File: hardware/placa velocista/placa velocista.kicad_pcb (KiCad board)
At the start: 2 copper layers, 103.6 x 74.9 mm, 22 parts, among them J1 Conn_01x07, J5 Screw_Terminal_01x02, SW2 SW_SPDT, SW3 s, U1 ESP32_CDN, U2 LM7805

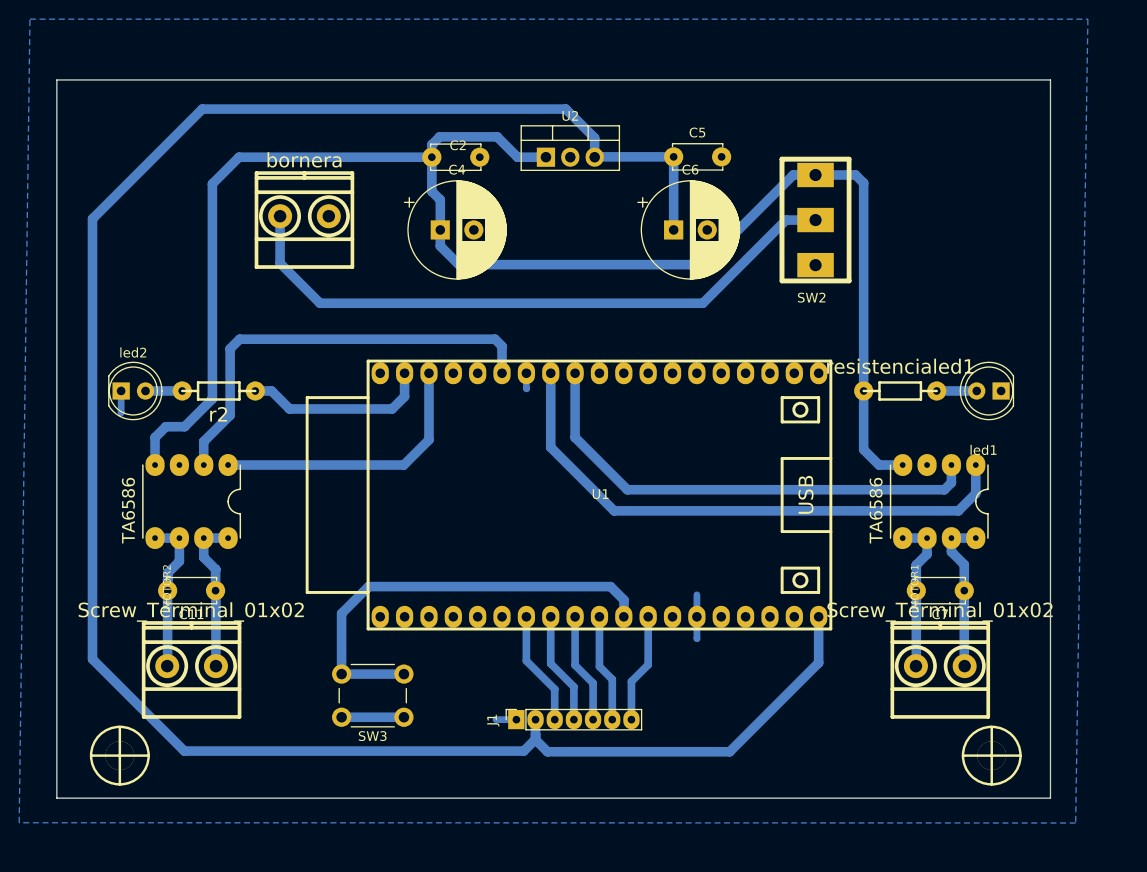
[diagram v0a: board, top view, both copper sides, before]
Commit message: Agregue divisor de tension
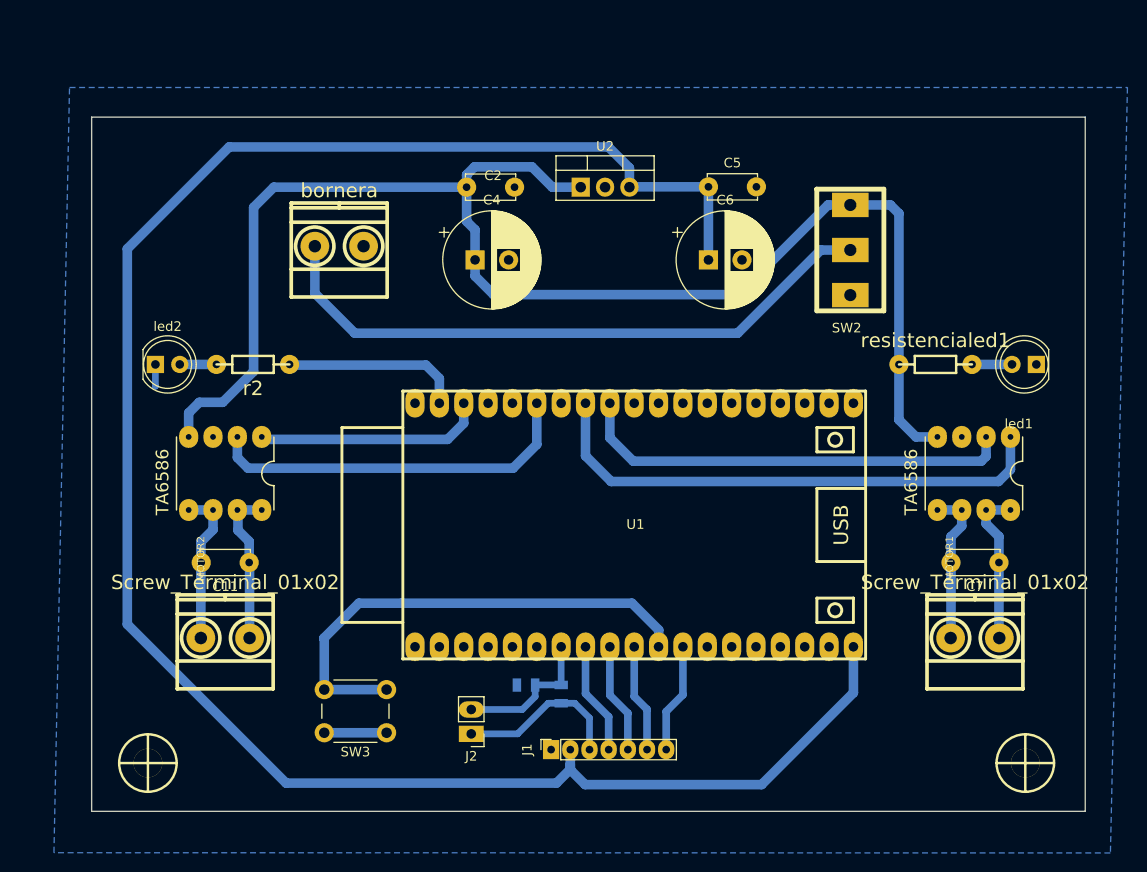
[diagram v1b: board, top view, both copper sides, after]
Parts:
- added J2: Conn_01x02, Connector_PinHeader_2.54mm:PinHeader_1x02_P2.54mm_Vertical, F.Cu at (62.8, 87.1)
- added R1: R, EESTN5:R_0805, B.Cu at (72.2, 82.9)
- added R3: R, EESTN5:R_0805, B.Cu at (68.6, 82.0)
- moved U1 4.79 mm to (79.8, 65.3)
- moved C2 4.79 mm to (62.4, 30.1)
- moved C4 4.79 mm to (63.2, 37.7)
- moved C5 4.79 mm to (87.6, 30.0)
- moved C6 4.79 mm to (87.6, 37.7)
- moved J1 4.79 mm to (71.2, 88.7)
- moved SW2 4.79 mm to (102.4, 36.6)
- moved U2 4.79 mm to (74.3, 30.1)
- moved bornerabateria1 4.79 mm to (49.1, 36.2)
- moved J5 4.65 mm to (115.4, 77.1)
- moved MOTOR1 4.65 mm to (112.7, 68.8)
- moved C7 4.65 mm to (117.9, 69.2)
- moved led1 4.60 mm to (121.8, 48.6)
- moved resistencialed1 4.60 mm to (111.3, 48.6)
- moved MOTOR2 4.57 mm to (34.6, 68.8)
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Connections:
- J1 pad 3: /OUT -> /OUTe
- U1 pad 7: /OUT -> /OUTs
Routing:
- net /OUTe: track 0.00 -> 17.6 mm
- net /OUTs: track 0.00 -> 15.1 mm
- net /OUT: track 11.9 -> 0.00 mm
- net VCC: track 163.1 -> 151.2 mm
- net GND: track 17.4 -> 8.78 mm
- net /DIRECCION4: track 45.2 -> 39.2 mm
- net Net-(SW3-B): track 46.1 -> 51.5 mm
- net /DIRECCION3: track 29.0 -> 24.0 mm
- net /DIRECCION2: track 50.4 -> 46.1 mm
- net +5V: track 214.2 -> 209.9 mm
- net /DIRECCION1: track 58.5 -> 54.8 mm
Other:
- board size 103.6 x 74.9 mm -> 103.6 x 72.4 mm
